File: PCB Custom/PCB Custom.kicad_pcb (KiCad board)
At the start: 2 copper layers, 15.3 x 20.4 mm, 0 parts

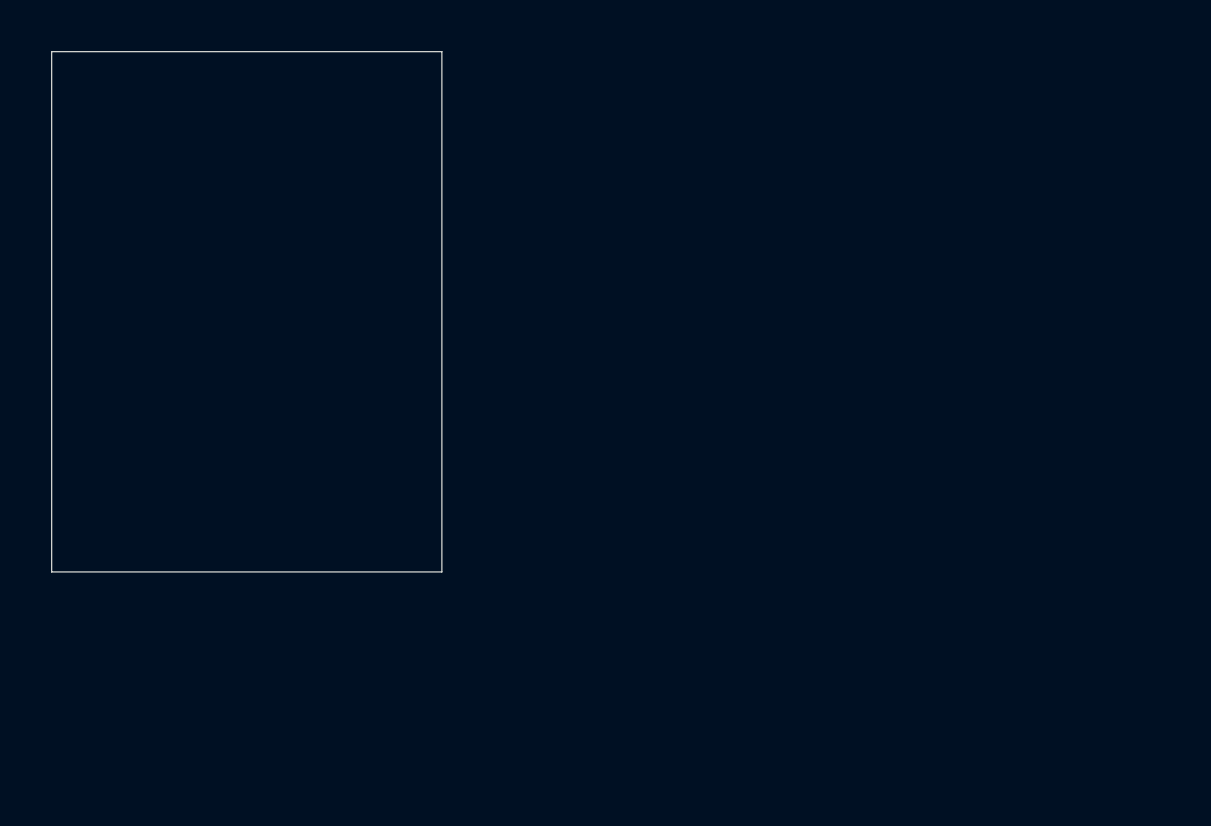
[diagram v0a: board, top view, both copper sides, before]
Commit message: added footprint from SparkFun TC78H670FTG as reference
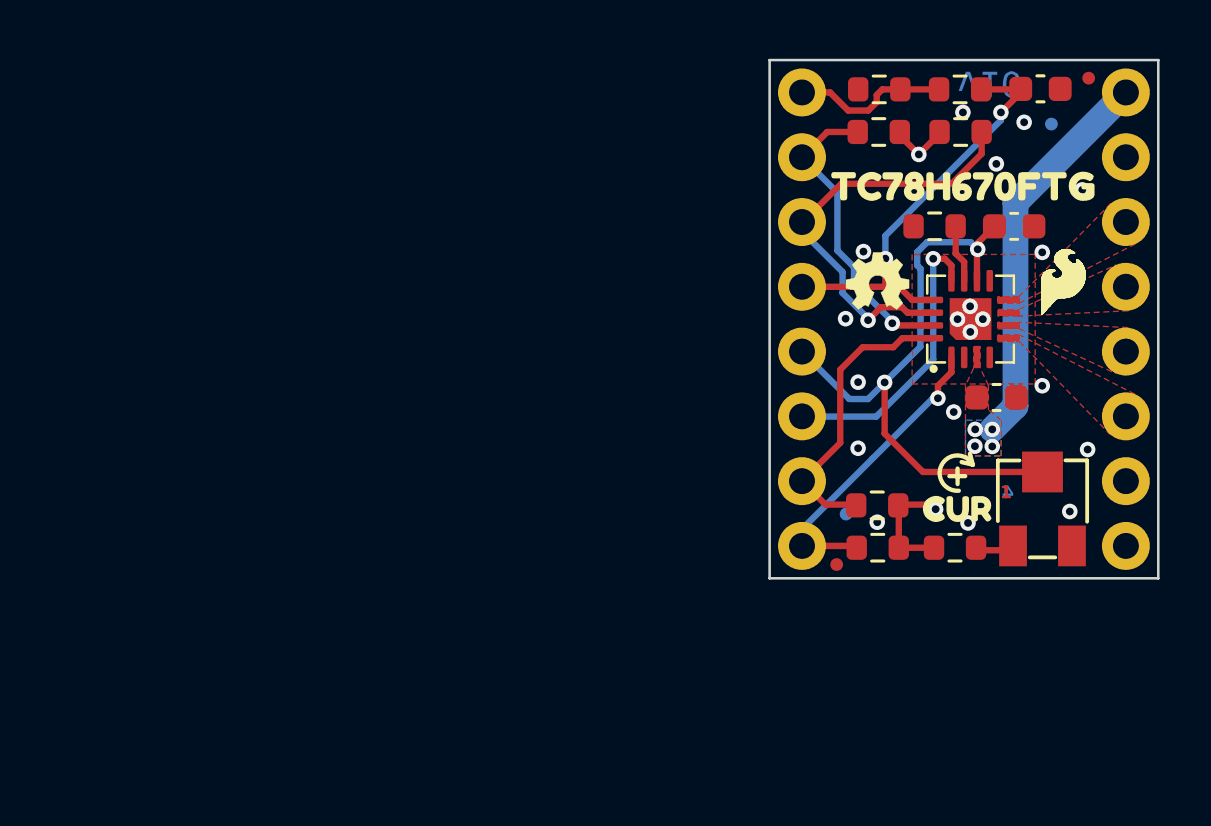
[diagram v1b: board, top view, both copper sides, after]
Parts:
- added C1: 0.1uF, SparkFun-Capacitor:C_0603_1608Metric, F.Cu at (117.3, 73.6)
- added C2: 0.1uF, SparkFun-Capacitor:C_0603_1608Metric, F.Cu at (118.0, 66.8)
- added C3: 22nF, SparkFun-Capacitor:C_0603_1608Metric, F.Cu at (119.0, 61.5)
- added FID1: Fiducial_0.5mm, SparkFun-Aesthetic:Fiducial_0.5mm_Mask1mm, F.Cu at (120.9, 61.0)
- added FID2: Fiducial_0.5mm, SparkFun-Aesthetic:Fiducial_0.5mm_Mask1mm, B.Cu at (111.4, 78.1)
- added FID3: Fiducial_0.5mm, SparkFun-Aesthetic:Fiducial_0.5mm_Mask1mm, B.Cu at (119.5, 62.8)
- added FID4: Fiducial_0.5mm, SparkFun-Aesthetic:Fiducial_0.5mm_Mask1mm, F.Cu at (111.0, 80.1)
- added G***: LOGO, SparkFun-Aesthetic:SparkFun_Logo_7mm, B.Cu at (115.3, 64.7)
- added J1: Conn_01x08, SparkFun-Connector:1x08, F.Cu at (109.7, 61.6)
- added J2: Conn_01x08, SparkFun-Connector:1X08, F.Cu at (122.4, 61.6)
- added R1: 8.2k, SparkFun-Resistor:R_0603_1608Metric, F.Cu at (115.7, 79.5)
- added R10: 47k, SparkFun-Resistor:R_0603_1608Metric, F.Cu at (114.9, 66.8)
- added R2: 10k, SparkFun-Resistor:Trimpot_SMD_3.0x3.0mm, F.Cu at (119.1, 77.9)
- added R3: 10k, SparkFun-Resistor:R_0603_1608Metric, F.Cu at (112.7, 61.5)
- added R4: 10k, SparkFun-Resistor:R_0603_1608Metric, F.Cu at (115.9, 61.5)
- added R5: 10k, SparkFun-Resistor:R_0603_1608Metric, F.Cu at (112.6, 79.5)
- added R7: 10k, SparkFun-Resistor:R_0603_1608Metric, F.Cu at (112.6, 77.8)
- added R8: 10k, SparkFun-Resistor:R_0603_1608Metric, F.Cu at (112.7, 63.1)
- added R9: 10k, SparkFun-Resistor:R_0603_1608Metric, F.Cu at (115.9, 63.1)
- added REF**: SFE_FLAME_0.1, SparkFun-Aesthetic:SFE_FLAME_0.1, F.Cu at (119.9, 69.1)
- added Ref**: Val**, SparkFun-Aesthetic:OSHW_Logo_2.5mm, F.Cu at (112.6, 69.1)
- added U1: TC78H670FTG, SparkFun-IC-Special-Function:P-VQFN16-0303-0.50-001, F.Cu at (117.0, 72.0)
- added kibuzzard-65CFAA22: G***, kibuzzard-65CFAA22, B.Cu at (120.2, 61.6)
- added kibuzzard-65CFAA33: G***, kibuzzard-65CFAA33, B.Cu at (119.8, 79.4)
- added kibuzzard-65CFAA33: G***, kibuzzard-65CFAA33, B.Cu at (119.8, 64.1)
- added kibuzzard-65CFAAF8: G***, kibuzzard-65CFAAF8, B.Cu at (119.9, 76.8)
- added kibuzzard-65CFAB5A: G***, kibuzzard-65CFAB5A, B.Cu at (120.1, 71.8)
- added kibuzzard-65CFAB77: G***, kibuzzard-65CFAB77, B.Cu at (120.2, 69.2)
- added kibuzzard-65CFAB85: G***, kibuzzard-65CFAB85, B.Cu at (120.1, 66.7)
- added kibuzzard-65CFAC13: G***, kibuzzard-65CFAC13, B.Cu at (112.1, 61.6)
- added kibuzzard-65CFAC2F: G***, kibuzzard-65CFAC2F, B.Cu at (112.0, 64.2)
- added kibuzzard-65CFAC42: G***, kibuzzard-65CFAC42, B.Cu at (112.2, 66.7)
- added kibuzzard-65CFAC5D: G***, kibuzzard-65CFAC5D, B.Cu at (112.5, 69.2)
- added kibuzzard-65CFAC9C: G***, kibuzzard-65CFAC9C, B.Cu at (112.9, 71.8)
- added kibuzzard-65CFAD2C: G***, kibuzzard-65CFAD2C, B.Cu at (112.8, 74.3)
- added kibuzzard-65CFAE3D: G***, kibuzzard-65CFAE3D, B.Cu at (120.0, 74.3)
- added kibuzzard-65CFAE6E: G***, kibuzzard-65CFAE6E, F.Cu at (116.0, 65.3)
- added kibuzzard-65CFAE6E: G***, kibuzzard-65CFAE6E, B.Cu at (116.9, 70.5)
- added kibuzzard-65D52B03: G***, kibuzzard-65D52B03, B.Cu at (113.8, 76.8)
- added kibuzzard-65D52B32: G***, kibuzzard-65D52B32, B.Cu at (113.2, 79.4)
- added kibuzzard-65D531EE: G***, kibuzzard-65D531EE, F.Cu at (115.8, 77.9)
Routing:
- net MISO: track 0.00 -> 23.9 mm, vias 0 -> 2
- net CS: track 0.00 -> 16.8 mm, vias 0 -> 2
- net SCK: track 0.00 -> 16.8 mm, vias 0 -> 1
- net VM: track 0.00 -> 15.4 mm, vias 0 -> 4
- net MOSI: track 0.00 -> 12.2 mm, vias 0 -> 1
- net DIR: track 0.00 -> 12.1 mm, vias 0 -> 1
- net STEP: track 0.00 -> 11.6 mm
- net ~{STBY}: track 0.00 -> 11.5 mm, vias 0 -> 1
- net 3.3V: track 0.00 -> 7.21 mm, vias 0 -> 2
- net EN: track 0.00 -> 6.18 mm
- net Net-(U1-OSCM): track 0.00 -> 2.27 mm
- net Net-(R1-Pad2): track 0.00 -> 1.73 mm
- net GND: vias 0 -> 19
- added copper zone on F.Cu, net A+
- added copper zone on F.Cu, net A-
- added copper zone on F.Cu, net B+
- added copper zone on F.Cu, net B-
- added copper zone on B.Cu, net GND
- added copper zone on F.Cu, net GND
- added copper zone on B.Cu, net VM
- added copper zone on F.Cu, net VM
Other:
- board size 15.3 x 20.4 mm -> 15.2 x 20.3 mm
- board text added: "1"
- board text added: "4"
- board text added: "v10"

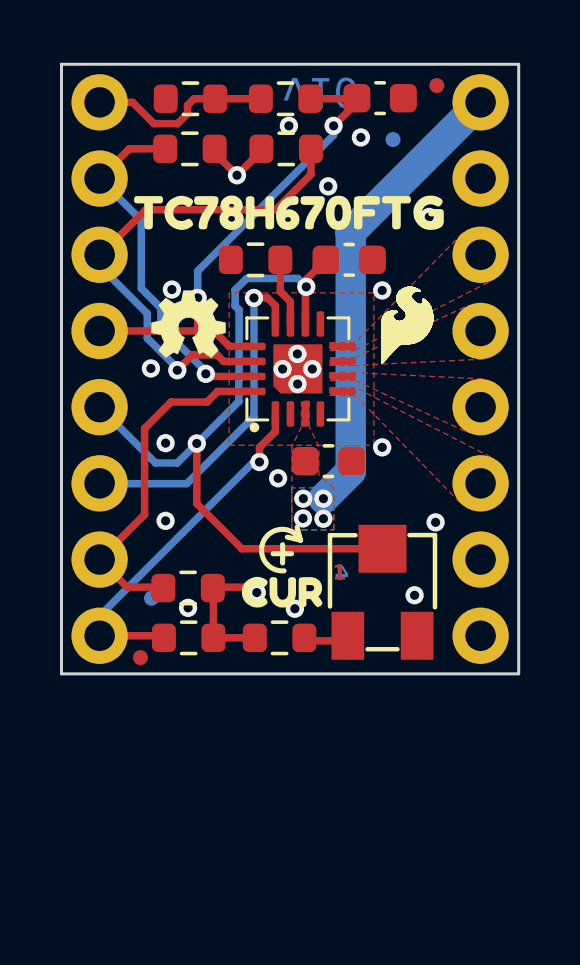
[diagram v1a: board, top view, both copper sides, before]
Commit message: added STEP files for custom PCB
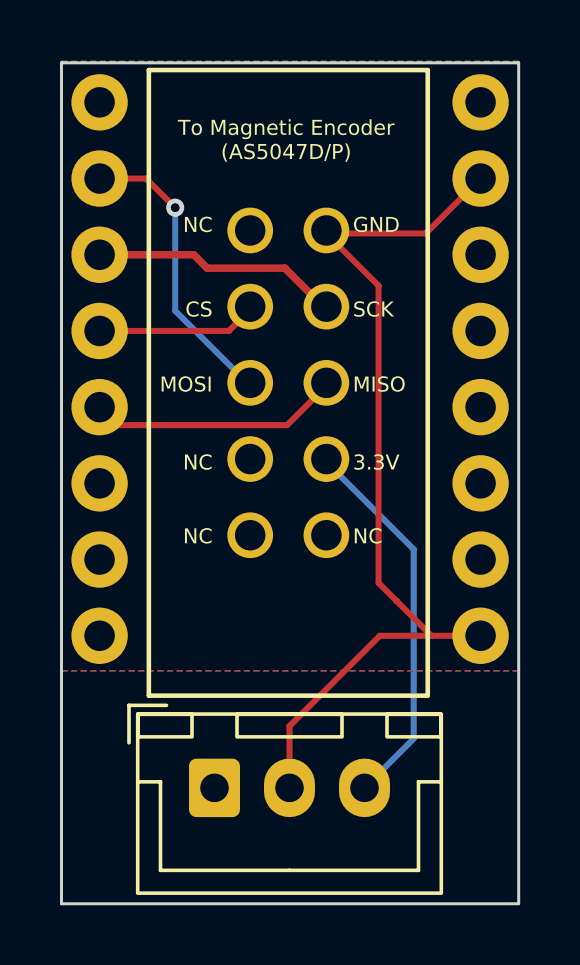
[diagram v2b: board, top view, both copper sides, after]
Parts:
- removed C1, C2: 0.1uF, SparkFun-Capacitor:C_0603_1608Metric
- removed C3: 22nF, SparkFun-Capacitor:C_0603_1608Metric
- removed FID1, FID2, FID3, FID4: Fiducial_0.5mm, SparkFun-Aesthetic:Fiducial_0.5mm_Mask1mm
- removed G***: LOGO, SparkFun-Aesthetic:SparkFun_Logo_7mm
- removed R1: 8.2k, SparkFun-Resistor:R_0603_1608Metric
- removed R10: 47k, SparkFun-Resistor:R_0603_1608Metric
- removed R2: 10k, SparkFun-Resistor:Trimpot_SMD_3.0x3.0mm
- removed R3, R4, R5, R7, R8, R9: 10k, SparkFun-Resistor:R_0603_1608Metric
- removed the REF** at (119.9, 69.1)
- removed Ref**: Val**, SparkFun-Aesthetic:OSHW_Logo_2.5mm
- removed U1: TC78H670FTG, SparkFun-IC-Special-Function:P-VQFN16-0303-0.50-001
- removed kibuzzard-65CFAA22: G***, kibuzzard-65CFAA22
- removed kibuzzard-65CFAA33 (x2): G***, kibuzzard-65CFAA33
- removed kibuzzard-65CFAAF8: G***, kibuzzard-65CFAAF8
- removed kibuzzard-65CFAB5A: G***, kibuzzard-65CFAB5A
- removed kibuzzard-65CFAB77: G***, kibuzzard-65CFAB77
- removed kibuzzard-65CFAB85: G***, kibuzzard-65CFAB85
- removed kibuzzard-65CFAC13: G***, kibuzzard-65CFAC13
- removed kibuzzard-65CFAC2F: G***, kibuzzard-65CFAC2F
- removed kibuzzard-65CFAC42: G***, kibuzzard-65CFAC42
- removed kibuzzard-65CFAC5D: G***, kibuzzard-65CFAC5D
- removed kibuzzard-65CFAC9C: G***, kibuzzard-65CFAC9C
- removed kibuzzard-65CFAD2C: G***, kibuzzard-65CFAD2C
- removed kibuzzard-65CFAE3D: G***, kibuzzard-65CFAE3D
- removed kibuzzard-65CFAE6E (x2): G***, kibuzzard-65CFAE6E
- removed kibuzzard-65D52B03: G***, kibuzzard-65D52B03
- removed kibuzzard-65D52B32: G***, kibuzzard-65D52B32
- removed kibuzzard-65D531EE: G***, kibuzzard-65D531EE
- added REF**: CONN10_302-S101_OST, 302-S101:CONN10_302-S101_OST, F.Cu at (114.7, 65.9)
- added REF**: JST_XH_B3B-XH-A_1x03_P2.50mm_Vertical, Connector_JST:JST_XH_B3B-XH-A_1x03_P2.50mm_Vertical, F.Cu at (113.5, 84.5)
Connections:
- J1 pad 6: ~{STBY} -> CLK
- J1 pad 7: STEP -> STP
- J2 pad 3: B+ -> A2
- J2 pad 4: B- -> A1
- J2 pad 5: A- -> B2
- J2 pad 6: A+ -> B1
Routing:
- net GND: track 0.00 -> 30.4 mm, vias 19 -> 0
- net MISO: track 23.9 -> 8.35 mm, vias 2 -> 0
- net VM: track 15.4 -> 0.00 mm, vias 4 -> 0
- net STEP: track 11.6 -> 0.00 mm
- net CS: track 16.8 -> 5.31 mm, vias 2 -> 0
- net ~{STBY}: track 11.5 -> 0.00 mm, vias 1 -> 0
- net DIR: track 12.1 -> 0.66 mm, vias 1 -> 0
- net SCK: track 16.8 -> 9.22 mm, vias 1 -> 0
- net EN: track 6.18 -> 0.00 mm
- net 3.3V: track 7.21 -> 12.7 mm, vias 2 -> 0
- net MOSI: track 12.2 -> 9.90 mm
- net Net-(U1-OSCM): track 2.27 -> 0.00 mm
- net Net-(R1-Pad2): track 1.73 -> 0.00 mm
- removed copper zone on F.Cu, net A+
- removed copper zone on F.Cu, net A-
- removed copper zone on F.Cu, net B+
- removed copper zone on F.Cu, net B-
- removed copper zone on B.Cu, net VM
- removed copper zone on F.Cu, net VM
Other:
- board size 15.2 x 20.3 mm -> 15.2 x 28 mm
- board text added: "3.3V"
- board text added: "CS"
- board text added: "GND"
- board text added: "MISO"
- board text added: "MOSI"
- board text added: "NC"
- board text added: "SCK"
- board text added: "To Magnetic Encoder (AS5047D/P)"
- board text removed: "1"
- board text removed: "4"
- board text removed: "v10"

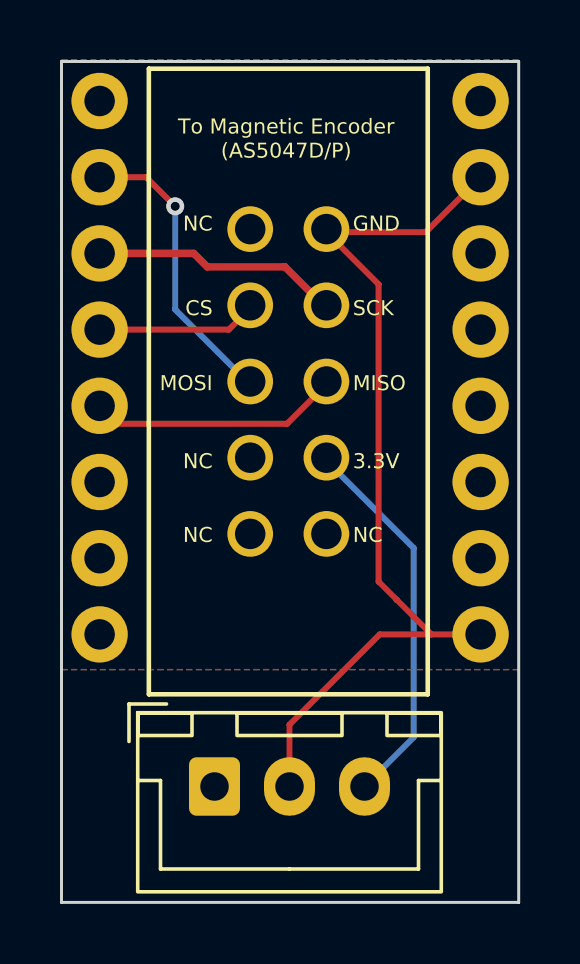
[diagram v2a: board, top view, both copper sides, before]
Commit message: stopped idle updates, improved placements of PCB traces
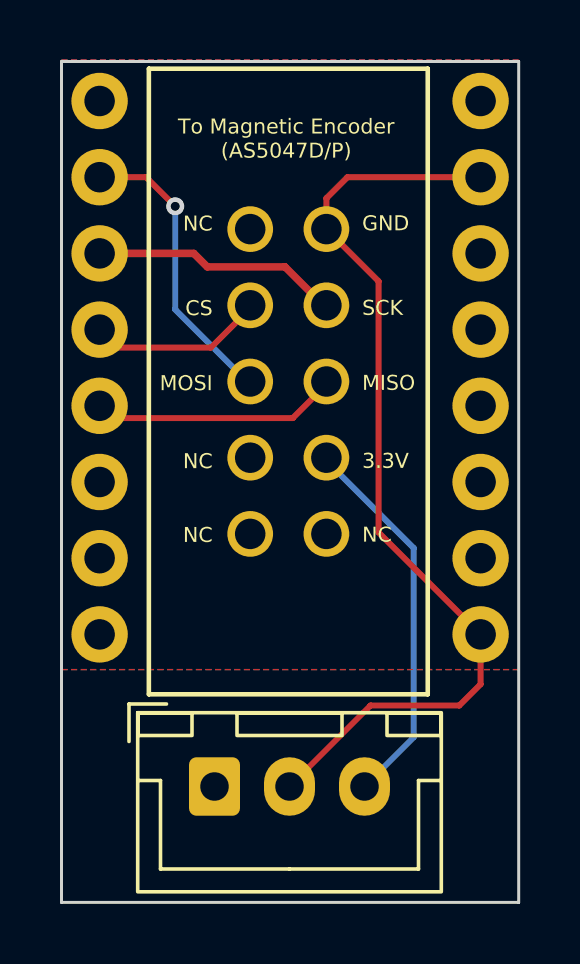
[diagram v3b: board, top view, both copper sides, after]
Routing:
- net GND: track 30.4 -> 32.2 mm
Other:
- board text added: "Built for BTT Octopus Pro v1.1"
- board text added: "Put into Stepper Motor Driver Sockets"
